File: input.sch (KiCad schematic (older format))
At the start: 8 parts

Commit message: Netlist and PCB generated
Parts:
- C1: renamed from C?; footprint (none) -> Capacitors_SMD:C_0805_HandSoldering
- P20, P21, P24, P25: renamed from P?; footprint (none) -> Pin_Headers:Pin_Header_Straight_1x01
- P22: renamed from P?; footprint (none) -> Pin_Headers:Pin_Header_Straight_1x02
- P23: renamed from P?; footprint (none) -> Pin_Headers:Pin_Header_Straight_2x05
- SW1: renamed from SW?; footprint (none) -> Buttons_Switches_SMD:SW_SPST_REED_CT05-XXXX-G1
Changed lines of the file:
@@
 $EndDescr
 $Comp
-L CONN_02X05 P?
+L CONN_02X05 P23
 U 1 1 57FDAB69
 P 1950 1100
-F 0 "P?" H 1950 1400 50  0000 C CNN
+F 0 "P23" H 1950 1400 50  0000 C CNN
 F 1 "SENOSRS_IN" H 1950 800 50  0000 C CNN
-F 2 "" H 1950 -100 50  0000 C CNN
+F 2 "Pin_Headers:Pin_Header_Straight_2x05" H 1950 -100 50  0001 C CNN
 F 3 "" H 1950 -100 50  0000 C CNN
 	1    1950 1100
@@
 $EndComp
 $Comp
-L GND #PWR?
+L GND #PWR014
 U 1 1 57FDABFE
 P 1000 1450
-F 0 "#PWR?" H 1000 1200 50  0001 C CNN
+F 0 "#PWR014" H 1000 1200 50  0001 C CNN
 F 1 "GND" H 1000 1300 50  0000 C CNN
 F 2 "" H 1000 1450 50  0000 C CNN
@@
 	2200 900  2250 900
 $Comp
-L CONN_01X01 P?
+L CONN_01X01 P20
 U 1 1 57FE1867
 P 1250 2200
-F 0 "P?" H 1250 2300 50  0000 C CNN
+F 0 "P20" H 1250 2300 50  0000 C CNN
 F 1 "5V+" V 1350 2200 50  0000 C CNN
-F 2 "" H 1250 2200 50  0000 C CNN
+F 2 "Pin_Headers:Pin_Header_Straight_1x01" H 1250 2200 50  0001 C CNN
 F 3 "" H 1250 2200 50  0000 C CNN
 	1    1250 2200
@@
 $EndComp
 $Comp
-L +5V #PWR?
+L +5V #PWR015
 U 1 1 57FE18D7
 P 1000 2150
-F 0 "#PWR?" H 1000 2000 50  0001 C CNN
+F 0 "#PWR015" H 1000 2000 50  0001 C CNN
 F 1 "+5V" H 1000 2290 50  0000 C CNN
 F 2 "" H 1000 2150 50  0000 C CNN
@@
 	1000 2200 1050 2200
 $Comp
-L CONN_01X01 P?
+L CONN_01X01 P21
 U 1 1 57FE1ADE
 P 1250 2400
-F 0 "P?" H 1250 2500 50  0000 C CNN
+F 0 "P21" H 1250 2500 50  0000 C CNN
 F 1 "5V-" V 1350 2400 50  0000 C CNN
-F 2 "" H 1250 2400 50  0000 C CNN
+F 2 "Pin_Headers:Pin_Header_Straight_1x01" H 1250 2400 50  0001 C CNN
 F 3 "" H 1250 2400 50  0000 C CNN
 	1    1250 2400
@@
 $EndComp
 $Comp
-L GND #PWR?
+L GND #PWR016
 U 1 1 57FE1B21
 P 1000 2500
-F 0 "#PWR?" H 1000 2250 50  0001 C CNN
+F 0 "#PWR016" H 1000 2250 50  0001 C CNN
 F 1 "GND" H 1000 2350 50  0000 C CNN
 F 2 "" H 1000 2500 50  0000 C CNN
@@
 	1000 2400 1000 2500
 $Comp
-L CONN_01X01 P?
+L CONN_01X01 P24
 U 1 1 57FE1DE8
 P 2400 2200
-F 0 "P?" H 2400 2300 50  0000 C CNN
+F 0 "P24" H 2400 2300 50  0000 C CNN
 F 1 "PSU_VIN" H 2600 2200 50  0000 C CNN
-F 2 "" H 2400 2200 50  0000 C CNN
+F 2 "Pin_Headers:Pin_Header_Straight_1x01" H 2400 2200 50  0001 C CNN
 F 3 "" H 2400 2200 50  0000 C CNN
 	1    2400 2200
@@
 $EndComp
 $Comp
-L CONN_01X01 P?
+L CONN_01X01 P25
 U 1 1 57FE1DF6
 P 2400 2400
-F 0 "P?" H 2400 2500 50  0000 C CNN
+F 0 "P25" H 2400 2500 50  0000 C CNN
 F 1 "PSU_VIN-" H 2650 2400 50  0000 C CNN
-F 2 "" H 2400 2400 50  0000 C CNN
+F 2 "Pin_Headers:Pin_Header_Straight_1x01" H 2400 2400 50  0001 C CNN
 F 3 "" H 2400 2400 50  0000 C CNN
 	1    2400 2400
@@
 $EndComp
 $Comp
-L CONN_01X02 P?
+L CONN_01X02 P22
 U 1 1 57FE2158
 P 1800 2300
-F 0 "P?" H 1800 2450 50  0000 C CNN
+F 0 "P22" H 1800 2450 50  0000 C CNN
 F 1 "PSU_TERMINAL_BLOCK" V 1900 2250 50  0000 C CNN
-F 2 "" H 1800 2300 50  0000 C CNN
+F 2 "Pin_Headers:Pin_Header_Straight_1x02" H 1800 2300 50  0001 C CNN
 F 3 "" H 1800 2300 50  0000 C CNN
 	1    1800 2300
@@
 	2050 2400 2200 2400
 $Comp
-L SW_PUSH_SMALL_H SW?
+L SW_PUSH_SMALL_H SW1
 U 1 1 57FE29DD
 P 1150 3150
-F 0 "SW?" H 1230 3260 50  0000 C CNN
+F 0 "SW1" H 1230 3260 50  0000 C CNN
 F 1 "RST" H 1150 3050 50  0000 C CNN
-F 2 "" H 1150 3350 50  0000 C CNN
+F 2 "Buttons_Switches_SMD:SW_SPST_REED_CT05-XXXX-G1" H 1150 3350 50  0001 C CNN
 F 3 "" H 1150 3350 50  0000 C CNN
 	1    1150 3150
@@
 $EndComp
 $Comp
-L C_Small C?
+L C_Small C1
 U 1 1 57FE2CD4
 P 1150 3400
-F 0 "C?" H 1160 3470 50  0000 L CNN
+F 0 "C1" H 1160 3470 50  0000 L CNN
 F 1 "100nF" H 1160 3320 50  0000 L CNN
-F 2 "" H 1150 3400 50  0000 C CNN
+F 2 "Capacitors_SMD:C_0805_HandSoldering" H 1150 3400 50  0001 C CNN
 F 3 "" H 1150 3400 50  0000 C CNN
 	1    1150 3400
@@
 	950  3400 950  3150
 Wire Wire Line
-	800  3150 950  3150
-Wire Wire Line
-	950  3150 1000 3150
+	800  3150 1000 3150
 Wire Wire Line
 	1250 3400 1350 3400
@@
 	1350 3400 1350 3150
 Wire Wire Line
-	1300 3150 1350 3150
-Wire Wire Line
-	1350 3150 1500 3150
+	1300 3150 1500 3150
 Text HLabel 800  3150 0    60   Input ~ 0
 RST
 Connection ~ 950  3150
 $Comp
-L GND #PWR?
+L GND #PWR017
 U 1 1 57FE30FD
 P 1500 3350
-F 0 "#PWR?" H 1500 3100 50  0001 C CNN
+F 0 "#PWR017" H 1500 3100 50  0001 C CNN
 F 1 "GND" H 1500 3200 50  0000 C CNN
 F 2 "" H 1500 3350 50  0000 C CNN

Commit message: PCB rev1.0
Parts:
- removed P22: PSU_TERMINAL_BLOCK, Pin_Headers:Pin_Header_Straight_1x02, symbol CONN_01X02
- removed P24: PSU_VIN, Pin_Headers:Pin_Header_Straight_1x01, symbol CONN_01X01
- removed P25: PSU_VIN-, Pin_Headers:Pin_Header_Straight_1x01, symbol CONN_01X01
- added P8: 5V_SERVO_JP, Socket_Strips:Socket_Strip_Straight_1x02, symbol CONN_01X02
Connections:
- net +5V: now also P8.2 (P2)
- net SENS_IN_0: now also P23.3 (P3); no longer P23.2 (P2)
- net SENS_IN_1: now also P23.5 (P5); no longer P23.3 (P3)
- net SENS_IN_2: now also P23.7 (P7); no longer P23.4 (P4)
- net SENS_IN_3: now also P23.9 (P9); no longer P23.5 (P5)
- net SENS_IN_4: now also P23.10 (P10); no longer P23.6 (P6)
- net SENS_IN_5: now also P23.8 (P8); no longer P23.7 (P7)
- net SENS_IN_6: now also P23.6 (P6); no longer P23.8 (P8)
- net SENS_IN_7: now also P23.4 (P4); no longer P23.9 (P9)
- net SENS_IN_8: now also P23.2 (P2); no longer P23.10 (P10)
- new net 5V_SERVO: P8.1 (P1)
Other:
- moved on the sheet: C1, SW1
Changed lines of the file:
@@
 $EndComp
 $Comp
-L GND #PWR014
+L GND #PWR010
 U 1 1 57FDABFE
 P 1000 1450
-F 0 "#PWR014" H 1000 1200 50  0001 C CNN
+F 0 "#PWR010" H 1000 1200 50  0001 C CNN
 F 1 "GND" H 1000 1300 50  0000 C CNN
 F 2 "" H 1000 1450 50  0000 C CNN
@@
 Wire Wire Line
 	1000 900  1700 900
+Text HLabel 1650 1100 0    60   Input ~ 0
+SENS_IN_1
+Text HLabel 1650 1300 0    60   Input ~ 0
+SENS_IN_3
+Text HLabel 2250 1200 2    60   Input ~ 0
+SENS_IN_5
+Text HLabel 2250 1000 2    60   Input ~ 0
+SENS_IN_7
 Text HLabel 1650 1000 0    60   Input ~ 0
-SENS_IN_1
-Text HLabel 1650 1100 0    60   Input ~ 0
-SENS_IN_3
+SENS_IN_0
 Text HLabel 1650 1200 0    60   Input ~ 0
-SENS_IN_5
-Text HLabel 1650 1300 0    60   Input ~ 0
-SENS_IN_7
+SENS_IN_2
+Text HLabel 2250 1300 2    60   Input ~ 0
+SENS_IN_4
+Text HLabel 2250 1100 2    60   Input ~ 0
+SENS_IN_6
 Text HLabel 2250 900  2    60   Input ~ 0
-SENS_IN_0
-Text HLabel 2250 1000 2    60   Input ~ 0
-SENS_IN_2
-Text HLabel 2250 1100 2    60   Input ~ 0
-SENS_IN_4
-Text HLabel 2250 1200 2    60   Input ~ 0
-SENS_IN_6
-Text HLabel 2250 1300 2    60   Input ~ 0
 SENS_IN_8
 Wire Wire Line
@@
 $EndComp
 $Comp
-L +5V #PWR015
+L +5V #PWR011
 U 1 1 57FE18D7
 P 1000 2150
-F 0 "#PWR015" H 1000 2000 50  0001 C CNN
+F 0 "#PWR011" H 1000 2000 50  0001 C CNN
 F 1 "+5V" H 1000 2290 50  0000 C CNN
 F 2 "" H 1000 2150 50  0000 C CNN
@@
 $EndComp
 $Comp
-L GND #PWR016
+L GND #PWR012
 U 1 1 57FE1B21
 P 1000 2500
-F 0 "#PWR016" H 1000 2250 50  0001 C CNN
+F 0 "#PWR012" H 1000 2250 50  0001 C CNN
 F 1 "GND" H 1000 2350 50  0000 C CNN
 F 2 "" H 1000 2500 50  0000 C CNN
@@
 	1000 2400 1000 2500
 $Comp
-L CONN_01X01 P24
-U 1 1 57FE1DE8
-P 2400 2200
-F 0 "P24" H 2400 2300 50  0000 C CNN
-F 1 "PSU_VIN" H 2600 2200 50  0000 C CNN
-F 2 "Pin_Headers:Pin_Header_Straight_1x01" H 2400 2200 50  0001 C CNN
-F 3 "" H 2400 2200 50  0000 C CNN
-	1    2400 2200
-	1    0    0    -1
-$EndComp
-$Comp
-L CONN_01X01 P25
-U 1 1 57FE1DF6
-P 2400 2400
-F 0 "P25" H 2400 2500 50  0000 C CNN
-F 1 "PSU_VIN-" H 2650 2400 50  0000 C CNN
-F 2 "Pin_Headers:Pin_Header_Straight_1x01" H 2400 2400 50  0001 C CNN
-F 3 "" H 2400 2400 50  0000 C CNN
-	1    2400 2400
-	1    0    0    -1
-$EndComp
-$Comp
-L CONN_01X02 P22
-U 1 1 57FE2158
-P 1800 2300
-F 0 "P22" H 1800 2450 50  0000 C CNN
-F 1 "PSU_TERMINAL_BLOCK" V 1900 2250 50  0000 C CNN
-F 2 "Pin_Headers:Pin_Header_Straight_1x02" H 1800 2300 50  0001 C CNN
-F 3 "" H 1800 2300 50  0000 C CNN
-	1    1800 2300
-	-1   0    0    -1
-$EndComp
-Wire Wire Line
-	2000 2250 2050 2250
-Wire Wire Line
-	2050 2250 2050 2200
-Wire Wire Line
-	2050 2200 2200 2200
-Wire Wire Line
-	2000 2350 2050 2350
-Wire Wire Line
-	2050 2350 2050 2400
-Wire Wire Line
-	2050 2400 2200 2400
-$Comp
 L SW_PUSH_SMALL_H SW1
 U 1 1 57FE29DD
-P 1150 3150
-F 0 "SW1" H 1230 3260 50  0000 C CNN
-F 1 "RST" H 1150 3050 50  0000 C CNN
-F 2 "Buttons_Switches_SMD:SW_SPST_REED_CT05-XXXX-G1" H 1150 3350 50  0001 C CNN
-F 3 "" H 1150 3350 50  0000 C CNN
-	1    1150 3150
+P 1375 3150
+F 0 "SW1" H 1455 3260 50  0000 C CNN
+F 1 "RST" H 1375 3050 50  0000 C CNN
+F 2 "Buttons_Switches_SMD:SW_SPST_REED_CT05-XXXX-G1" H 1375 3350 50  0001 C CNN
+F 3 "" H 1375 3350 50  0000 C CNN
+	1    1375 3150
 	1    0    0    -1
 $EndComp
@@
 L C_Small C1
 U 1 1 57FE2CD4
-P 1150 3400
-F 0 "C1" H 1160 3470 50  0000 L CNN
-F 1 "100nF" H 1160 3320 50  0000 L CNN
-F 2 "Capacitors_SMD:C_0805_HandSoldering" H 1150 3400 50  0001 C CNN
-F 3 "" H 1150 3400 50  0000 C CNN
-	1    1150 3400
+P 1375 3400
+F 0 "C1" H 1385 3470 50  0000 L CNN
+F 1 "100nF" H 1385 3320 50  0000 L CNN
+F 2 "Capacitors_SMD:C_0805_HandSoldering" H 1375 3400 50  0001 C CNN
+F 3 "" H 1375 3400 50  0000 C CNN
+	1    1375 3400
 	0    1    1    0
 $EndComp
 Wire Wire Line
-	1050 3400 950  3400
+	1275 3400 1175 3400
 Wire Wire Line
-	950  3400 950  3150
+	1175 3400 1175 3150
 Wire Wire Line
-	800  3150 1000 3150
+	1025 3150 1225 3150
 Wire Wire Line
-	1250 3400 1350 3400
+	1475 3400 1575 3400
 Wire Wire Line
-	1350 3400 1350 3150
+	1575 3400 1575 3150
 Wire Wire Line
-	1300 3150 1500 3150
-Text HLabel 800  3150 0    60   Input ~ 0
+	1525 3150 1725 3150
+Text HLabel 1025 3150 0    60   Input ~ 0
 RST
-Connection ~ 950  3150
+Connection ~ 1175 3150
 $Comp
-L GND #PWR017
+L GND #PWR013
 U 1 1 57FE30FD
-P 1500 3350
-F 0 "#PWR017" H 1500 3100 50  0001 C CNN
-F 1 "GND" H 1500 3200 50  0000 C CNN
-F 2 "" H 1500 3350 50  0000 C CNN
-F 3 "" H 1500 3350 50  0000 C CNN
-	1    1500 3350
+P 1725 3350
+F 0 "#PWR013" H 1725 3100 50  0001 C CNN
+F 1 "GND" H 1725 3200 50  0000 C CNN
+F 2 "" H 1725 3350 50  0000 C CNN
+F 3 "" H 1725 3350 50  0000 C CNN
+	1    1725 3350
 	1    0    0    -1
 $EndComp
 Wire Wire Line
-	1500 3150 1500 3350
-Connection ~ 1350 3150
+	1725 3150 1725 3350
+Connection ~ 1575 3150
+$Comp
+L CONN_01X02 P8
+U 1 1 57FEDB28
+P 1400 4225
+F 0 "P8" H 1400 4375 50  0000 C CNN
+F 1 "5V_SERVO_JP" V 1500 4225 50  0000 C CNN
+F 2 "Socket_Strips:Socket_Strip_Straight_1x02" H 1400 4225 50  0001 C CNN
+F 3 "" H 1400 4225 50  0000 C CNN
+	1    1400 4225
+	0    1    1    0
+$EndComp
+$Comp
+L +5V #PWR014
+U 1 1 57FEDDD4
+P 1350 3950
+F 0 "#PWR014" H 1350 3800 50  0001 C CNN
+F 1 "+5V" H 1350 4090 50  0000 C CNN
+F 2 "" H 1350 3950 50  0000 C CNN
+F 3 "" H 1350 3950 50  0000 C CNN
+	1    1350 3950
+	1    0    0    -1
+$EndComp
+Wire Wire Line
+	1350 3950 1350 4025
+Text GLabel 1525 3900 2    60   Input ~ 0
+5V_SERVO
+Wire Wire Line
+	1450 4025 1450 3900
+Wire Wire Line
+	1450 3900 1525 3900
 $EndSCHEMATC

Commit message: pcb rev2
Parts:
- removed P20: 5V+, Pin_Headers:Pin_Header_Straight_1x01, symbol CONN_01X01
- removed P21: 5V-, Pin_Headers:Pin_Header_Straight_1x01, symbol CONN_01X01
- added P10: CONN_2, Terminal_Blocks:TerminalBlock_Pheonix_MKDS1.5-2pol, symbol CONN_2
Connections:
- net +5V: now also P10.1 (P1)
- net GND: now also P10.2 (P2)
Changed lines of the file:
@@
 LIBS:contrib
 LIBS:valves
+LIBS:borniers
 LIBS:Arduino_Mega-cache
 EELAYER 25 0
@@
 	2200 900  2250 900
 $Comp
-L CONN_01X01 P20
-U 1 1 57FE1867
-P 1250 2200
-F 0 "P20" H 1250 2300 50  0000 C CNN
-F 1 "5V+" V 1350 2200 50  0000 C CNN
-F 2 "Pin_Headers:Pin_Header_Straight_1x01" H 1250 2200 50  0001 C CNN
-F 3 "" H 1250 2200 50  0000 C CNN
-	1    1250 2200
-	1    0    0    -1
-$EndComp
-$Comp
 L +5V #PWR011
 U 1 1 57FE18D7
-P 1000 2150
-F 0 "#PWR011" H 1000 2000 50  0001 C CNN
-F 1 "+5V" H 1000 2290 50  0000 C CNN
-F 2 "" H 1000 2150 50  0000 C CNN
-F 3 "" H 1000 2150 50  0000 C CNN
-	1    1000 2150
-	1    0    0    -1
-$EndComp
-Wire Wire Line
-	1000 2150 1000 2200
-Wire Wire Line
-	1000 2200 1050 2200
-$Comp
-L CONN_01X01 P21
-U 1 1 57FE1ADE
-P 1250 2400
-F 0 "P21" H 1250 2500 50  0000 C CNN
-F 1 "5V-" V 1350 2400 50  0000 C CNN
-F 2 "Pin_Headers:Pin_Header_Straight_1x01" H 1250 2400 50  0001 C CNN
-F 3 "" H 1250 2400 50  0000 C CNN
-	1    1250 2400
-	1    0    0    -1
-$EndComp
+P 1200 2100
+F 0 "#PWR011" H 1200 1950 50  0001 C CNN
+F 1 "+5V" H 1200 2240 50  0000 C CNN
+F 2 "" H 1200 2100 50  0000 C CNN
+F 3 "" H 1200 2100 50  0000 C CNN
+	1    1200 2100
+	1    0    0    -1
+$EndComp
+Wire Wire Line
+	1200 2100 1200 2150
+Wire Wire Line
+	1200 2150 1250 2150
 $Comp
 L GND #PWR012
 U 1 1 57FE1B21
-P 1000 2500
-F 0 "#PWR012" H 1000 2250 50  0001 C CNN
-F 1 "GND" H 1000 2350 50  0000 C CNN
-F 2 "" H 1000 2500 50  0000 C CNN
-F 3 "" H 1000 2500 50  0000 C CNN
-	1    1000 2500
-	1    0    0    -1
-$EndComp
-Wire Wire Line
-	1050 2400 1000 2400
-Wire Wire Line
-	1000 2400 1000 2500
+P 1200 2450
+F 0 "#PWR012" H 1200 2200 50  0001 C CNN
+F 1 "GND" H 1200 2300 50  0000 C CNN
+F 2 "" H 1200 2450 50  0000 C CNN
+F 3 "" H 1200 2450 50  0000 C CNN
+	1    1200 2450
+	1    0    0    -1
+$EndComp
+Wire Wire Line
+	1250 2350 1200 2350
+Wire Wire Line
+	1200 2350 1200 2450
 $Comp
 L SW_PUSH_SMALL_H SW1
@@
 Wire Wire Line
 	1450 3900 1525 3900
+$Comp
+L CONN_2 P10
+U 1 1 57FFF850
+P 1600 2250
+F 0 "P10" V 1550 2250 40  0000 C CNN
+F 1 "CONN_2" V 1650 2250 40  0000 C CNN
+F 2 "Terminal_Blocks:TerminalBlock_Pheonix_MKDS1.5-2pol" H 1600 2250 60  0001 C CNN
+F 3 "" H 1600 2250 60  0001 C CNN
+	1    1600 2250
+	1    0    0    -1
+$EndComp
 $EndSCHEMATC

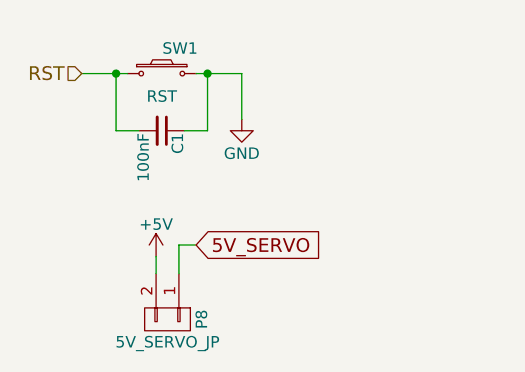
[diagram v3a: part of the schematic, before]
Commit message: Jumper removed, pdf generated
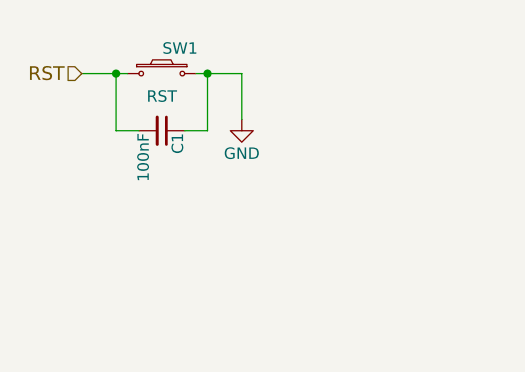
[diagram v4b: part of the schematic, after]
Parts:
- removed P8: 5V_SERVO_JP, Socket_Strips:Socket_Strip_Straight_1x02, symbol CONN_01X02
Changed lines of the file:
@@
 Connection ~ 1575 3150
-$Comp
-L CONN_01X02 P8
-U 1 1 57FEDB28
-P 1400 4225
-F 0 "P8" H 1400 4375 50  0000 C CNN
-F 1 "5V_SERVO_JP" V 1500 4225 50  0000 C CNN
-F 2 "Socket_Strips:Socket_Strip_Straight_1x02" H 1400 4225 50  0001 C CNN
-F 3 "" H 1400 4225 50  0000 C CNN
-	1    1400 4225
-	0    1    1    0
-$EndComp
-$Comp
-L +5V #PWR014
-U 1 1 57FEDDD4
-P 1350 3950
-F 0 "#PWR014" H 1350 3800 50  0001 C CNN
-F 1 "+5V" H 1350 4090 50  0000 C CNN
-F 2 "" H 1350 3950 50  0000 C CNN
-F 3 "" H 1350 3950 50  0000 C CNN
-	1    1350 3950
-	1    0    0    -1
-$EndComp
-Wire Wire Line
-	1350 3950 1350 4025
-Text GLabel 1525 3900 2    60   Input ~ 0
-5V_SERVO
-Wire Wire Line
-	1450 4025 1450 3900
-Wire Wire Line
-	1450 3900 1525 3900
 $Comp
 L CONN_2 P10
